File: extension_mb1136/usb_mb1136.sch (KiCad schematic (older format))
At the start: 20 parts, among them J1 Conn_01x03, J2 Conn_01x03, Q1 S9013, U1 STMPS2151MTR, U2 USBLC6-2

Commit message: add connector, develop pcb
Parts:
- added CNUSB_?: USB_B, Connector_USB:USB_B_OST_USB-B1HSxx_Horizontal, symbol Connector:USB_B
- renumbered C1 to C?, CNUSB_1 to CNUSB_?, CNUSB_2 to CNUSB_?, D1 to D?, LD1 to LD?, LD2 to LD?, Q1 to Q?, R1 to R?, R2 to R?, R5 to R?, R7 to R?, R4 to R?, R6 to R?, R8 to R?, R3 to R?, R9 to R?, U2 to U?, U1 to U?
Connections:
- net GND: now also CNUSB_?.4 (GND), CNUSB_?.5 (Shield)
- net at CNUSB_?.2 (D-), CNUSB_?.2 (D-), U?.4 (DMOUT): now also CNUSB_?.2 (D-)
- net at CNUSB_?.3 (D+), CNUSB_?.3 (D+), U?.6 (DPOUT): now also CNUSB_?.3 (D+)
- net VBUS renamed PA9
- net PA9: now also CNUSB_?.1 (VBUS)
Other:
- moved on the sheet: CNUSB_?

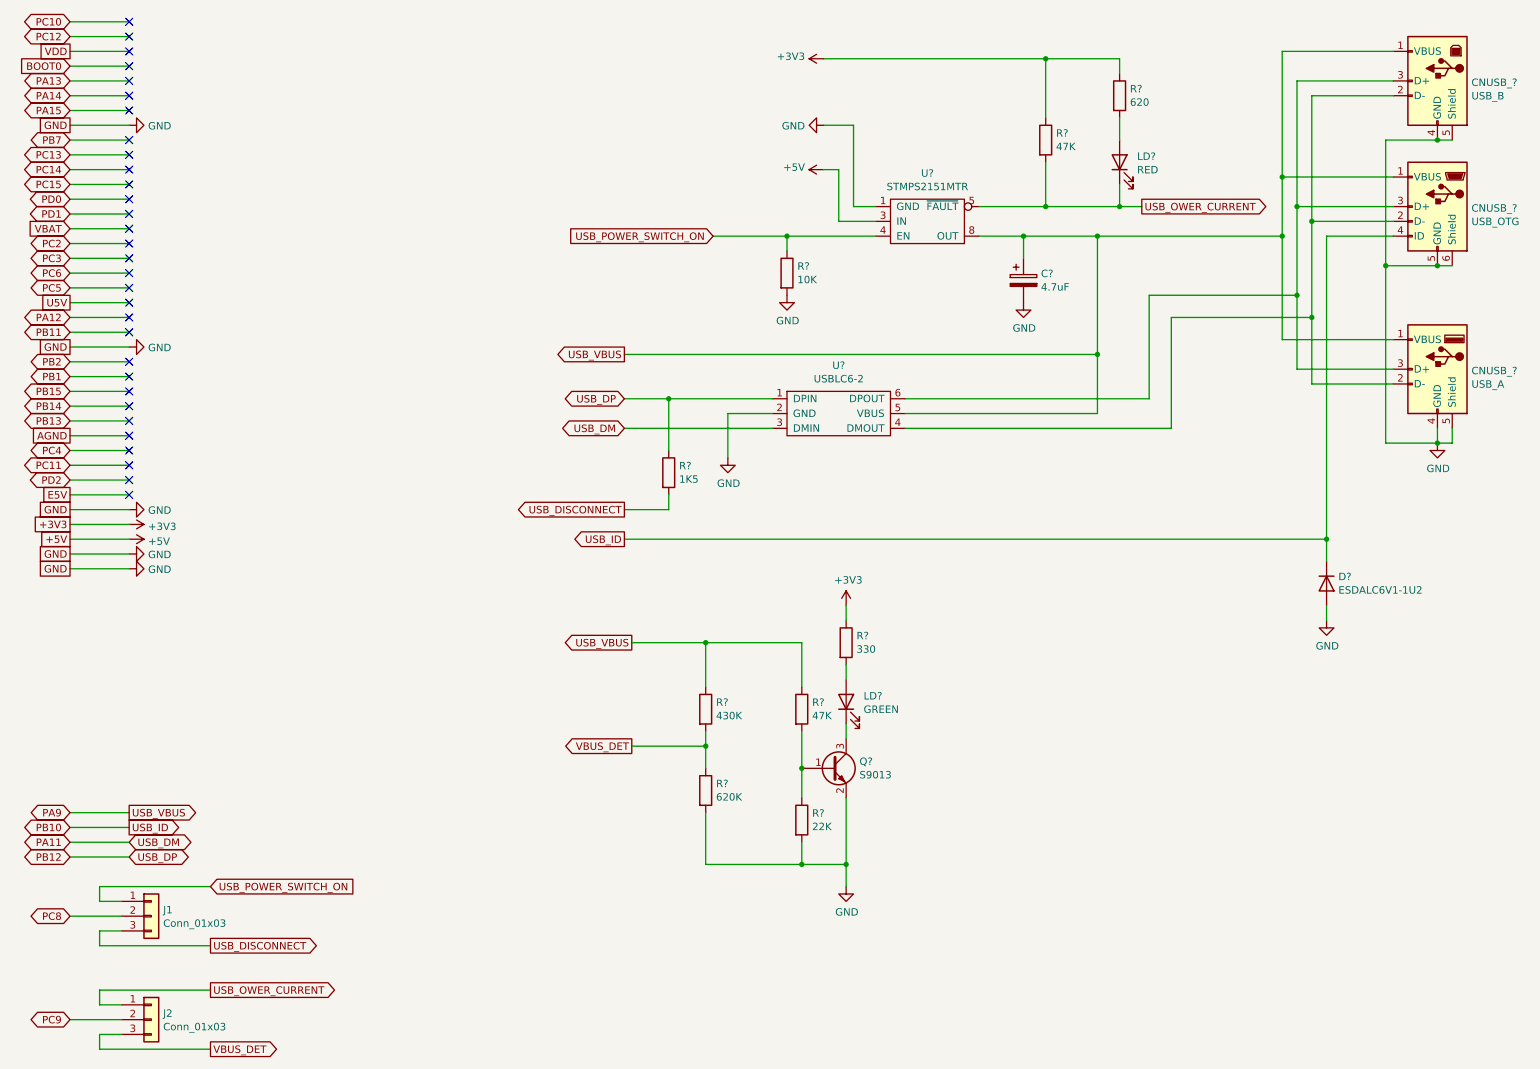
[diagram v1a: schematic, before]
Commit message: restore number of element
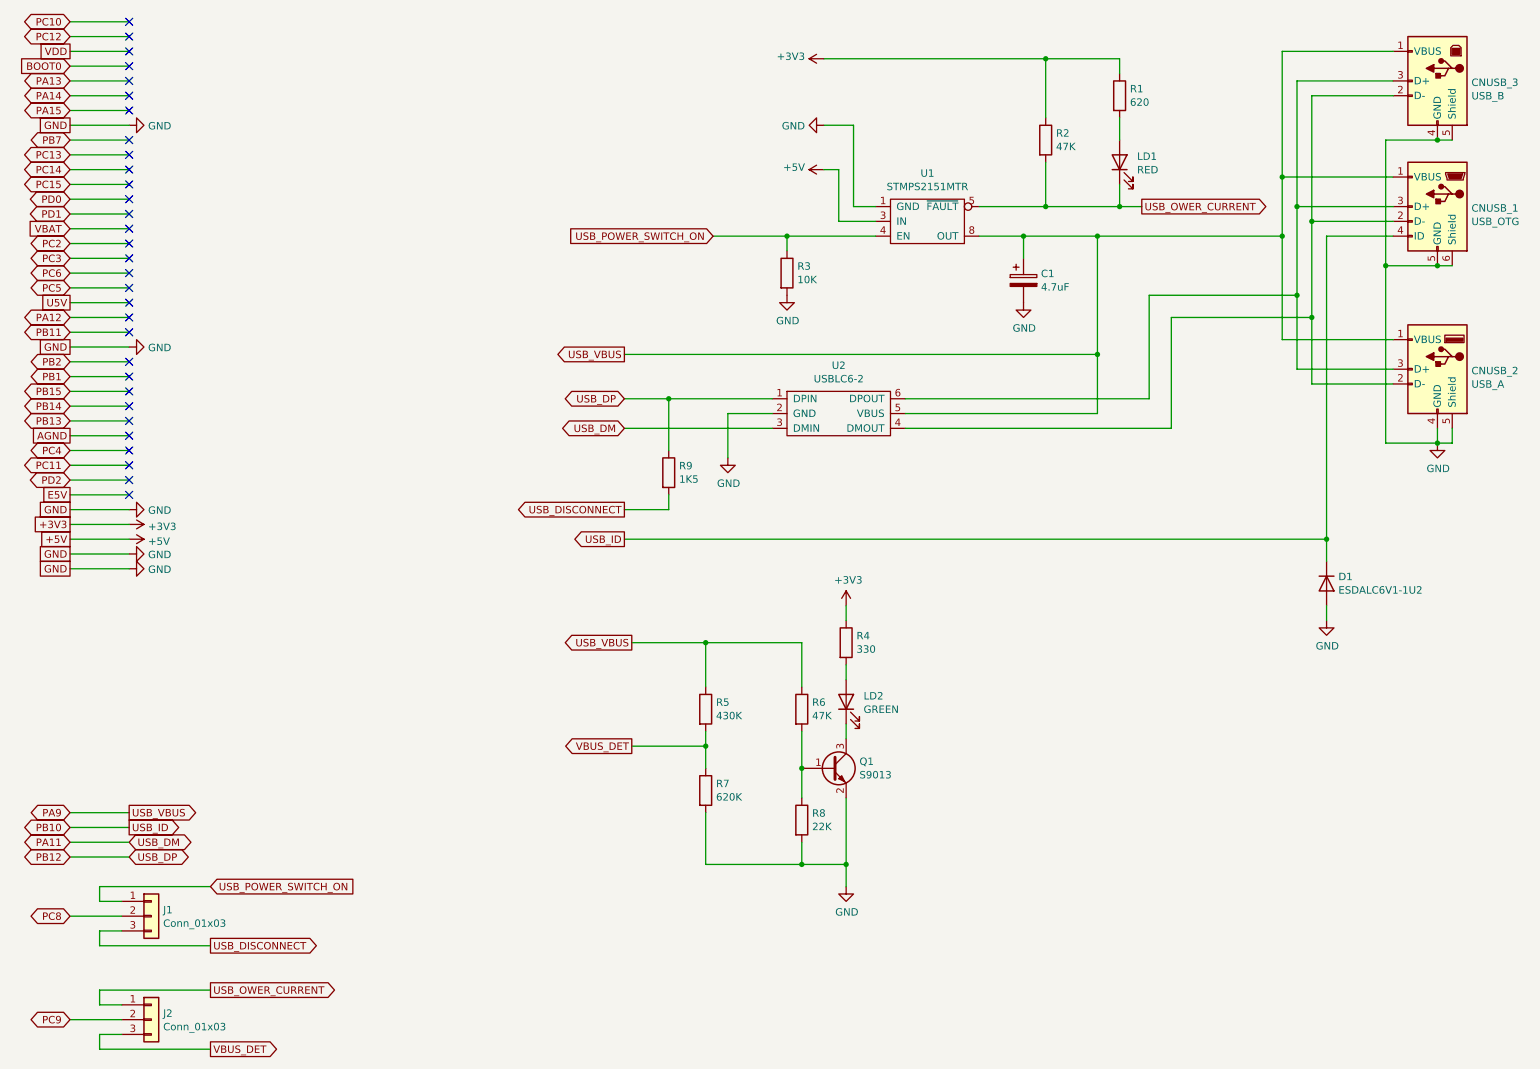
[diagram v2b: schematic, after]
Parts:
- gave numbers to parts that had none: 19
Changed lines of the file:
@@
 $EndDescr
 $Comp
-L Connector:USB_OTG CNUSB_?
+L Connector:USB_OTG CNUSB_1
 U 1 1 5FBD271C
 P 10150 1900
-F 0 "CNUSB_?" H 9920 1889 50  0000 R CNN
+F 0 "CNUSB_1" H 9920 1889 50  0000 R CNN
 F 1 "USB_OTG" H 9920 1798 50  0000 R CNN
 F 2 "Connector_USB:USB_Micro-B_Molex-105017-0001" H 10300 1850 50  0001 C CNN
@@
 USB_POWER_SWITCH_ON
 $Comp
-L Connector:USB_A CNUSB_?
+L Connector:USB_A CNUSB_2
 U 1 1 5FF0ECB3
 P 10150 3000
-F 0 "CNUSB_?" H 9920 2989 50  0000 R CNN
+F 0 "CNUSB_2" H 9920 2989 50  0000 R CNN
 F 1 "USB_A" H 9920 2898 50  0000 R CNN
 F 2 "Connector_USB:USB_A_Molex_67643_Horizontal" H 10300 2950 50  0001 C CNN
@@
 	10250 3500 10150 3500
 $Comp
-L Device:R R?
+L Device:R R1
 U 1 1 5FF1C87A
 P 8000 1150
-F 0 "R?" H 8070 1196 50  0000 L CNN
+F 0 "R1" H 8070 1196 50  0000 L CNN
 F 1 "620" H 8070 1105 50  0000 L CNN
 F 2 "Resistor_SMD:R_0805_2012Metric" V 7930 1150 50  0001 C CNN
@@
 $EndComp
 $Comp
-L Device:CP C?
+L Device:CP C1
 U 1 1 5FF205B2
 P 7350 2400
-F 0 "C?" H 7468 2446 50  0000 L CNN
+F 0 "C1" H 7468 2446 50  0000 L CNN
 F 1 "4.7uF" H 7468 2355 50  0000 L CNN
 F 2 "Capacitor_SMD:C_1206_3216Metric" H 7388 2250 50  0001 C CNN
@@
 $EndComp
 $Comp
-L power:GND #PWR?
+L power:GND #PWR0106
 U 1 1 5FF233E8
 P 7350 2550
-F 0 "#PWR?" H 7350 2300 50  0001 C CNN
+F 0 "#PWR0106" H 7350 2300 50  0001 C CNN
 F 1 "GND" H 7355 2377 50  0000 C CNN
 F 2 "" H 7350 2550 50  0001 C CNN
@@
 Connection ~ 7350 2100
 $Comp
-L Device:LED LD?
+L Device:LED LD1
 U 1 1 5FF25C2F
 P 8000 1600
-F 0 "LD?" V 8039 1482 50  0000 R CNN
+F 0 "LD1" V 8039 1482 50  0000 R CNN
 F 1 "RED" V 7948 1482 50  0000 R CNN
 F 2 "Diode_SMD:D_0805_2012Metric" H 8000 1600 50  0001 C CNN
@@
 Connection ~ 8000 1900
 $Comp
-L Device:R R?
+L Device:R R2
 U 1 1 5FF305D1
 P 7500 1450
-F 0 "R?" H 7570 1496 50  0000 L CNN
+F 0 "R2" H 7570 1496 50  0000 L CNN
 F 1 "47K" H 7570 1405 50  0000 L CNN
 F 2 "Resistor_SMD:R_0805_2012Metric" V 7430 1450 50  0001 C CNN
@@
 	7500 900  7500 1300
 $Comp
-L Device:R R?
+L Device:R R5
 U 1 1 5FF38FC2
 P 5200 5300
-F 0 "R?" H 5270 5346 50  0000 L CNN
+F 0 "R5" H 5270 5346 50  0000 L CNN
 F 1 "430K" H 5270 5255 50  0000 L CNN
 F 2 "Resistor_SMD:R_0805_2012Metric" V 5130 5300 50  0001 C CNN
@@
 $EndComp
 $Comp
-L Device:R R?
+L Device:R R7
 U 1 1 5FF3EEB0
 P 5200 5850
-F 0 "R?" H 5270 5896 50  0000 L CNN
+F 0 "R7" H 5270 5896 50  0000 L CNN
 F 1 "620K" H 5270 5805 50  0000 L CNN
 F 2 "Resistor_SMD:R_0805_2012Metric" V 5130 5850 50  0001 C CNN
@@
 VBUS_DET
 $Comp
-L Device:Q_NPN_BEC Q?
+L Device:Q_NPN_BEC Q1
 U 1 1 5FF6C39D
 P 6050 5700
-F 0 "Q?" H 6240 5746 50  0000 L CNN
+F 0 "Q1" H 6240 5746 50  0000 L CNN
 F 1 "S9013" H 6240 5655 50  0000 L CNN
 F 2 "Package_TO_SOT_SMD:SOT-23" H 6250 5800 50  0001 C CNN
@@
 Connection ~ 7850 2100
 $Comp
-L Device:R R?
+L Device:R R4
 U 1 1 5FF7C0A5
 P 6150 4850
-F 0 "R?" H 6220 4896 50  0000 L CNN
+F 0 "R4" H 6220 4896 50  0000 L CNN
 F 1 "330" H 6220 4805 50  0000 L CNN
 F 2 "Resistor_SMD:R_0805_2012Metric" V 6080 4850 50  0001 C CNN
@@
 $EndComp
 $Comp
-L Device:LED LD?
+L Device:LED LD2
 U 1 1 5FF7C0AB
 P 6150 5250
-F 0 "LD?" V 6189 5132 50  0000 R CNN
+F 0 "LD2" V 6189 5132 50  0000 R CNN
 F 1 "GREEN" V 6098 5132 50  0000 R CNN
 F 2 "Diode_SMD:D_0805_2012Metric" H 6150 5250 50  0001 C CNN
@@
 $EndComp
 $Comp
-L Device:R R?
+L Device:R R6
 U 1 1 5FF89CAE
 P 5850 5300
-F 0 "R?" H 5920 5346 50  0000 L CNN
+F 0 "R6" H 5920 5346 50  0000 L CNN
 F 1 "47K" H 5920 5255 50  0000 L CNN
 F 2 "Resistor_SMD:R_0805_2012Metric" V 5780 5300 50  0001 C CNN
@@
 	9100 2800 9100 2100
 $Comp
-L power:+3V3 #PWR?
+L power:+3V3 #PWR0101
 U 1 1 5FFAAE95
 P 6150 4600
-F 0 "#PWR?" H 6150 4450 50  0001 C CNN
+F 0 "#PWR0101" H 6150 4450 50  0001 C CNN
 F 1 "+3V3" H 6165 4773 50  0000 C CNN
 F 2 "" H 6150 4600 50  0001 C CNN
@@
 	6150 4600 6150 4700
 $Comp
-L power:GND #PWR?
+L power:GND #PWR0101
 U 1 1 5FFB903B
 P 6150 6500
-F 0 "#PWR?" H 6150 6250 50  0001 C CNN
+F 0 "#PWR0101" H 6150 6250 50  0001 C CNN
 F 1 "GND" H 6155 6327 50  0000 C CNN
 F 2 "" H 6150 6500 50  0001 C CNN
@@
 $EndComp
 $Comp
-L Device:R R?
+L Device:R R8
 U 1 1 5FFBBFDE
 P 5850 6050
-F 0 "R?" H 5920 6096 50  0000 L CNN
+F 0 "R8" H 5920 6096 50  0000 L CNN
 F 1 "22K" H 5920 6005 50  0000 L CNN
 F 2 "Resistor_SMD:R_0805_2012Metric" V 5780 6050 50  0001 C CNN
@@
 	5250 2100 5750 2100
 $Comp
-L Device:R R?
+L Device:R R3
 U 1 1 60084099
 P 5750 2350
-F 0 "R?" H 5820 2396 50  0000 L CNN
+F 0 "R3" H 5820 2396 50  0000 L CNN
 F 1 "10K" H 5820 2305 50  0000 L CNN
 F 2 "Resistor_SMD:R_0805_2012Metric" V 5680 2350 50  0001 C CNN
@@
 $EndComp
 $Comp
-L power:GND #PWR?
+L power:GND #PWR0111
 U 1 1 6008AD44
 P 5750 2500
-F 0 "#PWR?" H 5750 2250 50  0001 C CNN
+F 0 "#PWR0111" H 5750 2250 50  0001 C CNN
 F 1 "GND" H 5755 2327 50  0000 C CNN
 F 2 "" H 5750 2500 50  0001 C CNN
@@
 	9400 4150 4650 4150
 $Comp
-L Device:D D?
+L Device:D D1
 U 1 1 600DB0FD
 P 9400 4450
-F 0 "D?" V 9354 4530 50  0000 L CNN
+F 0 "D1" V 9354 4530 50  0000 L CNN
 F 1 "ESDALC6V1-1U2" V 9445 4530 50  0000 L CNN
 F 2 "Diode_SMD:D_0201_0603Metric" H 9400 4450 50  0001 C CNN
@@
 Connection ~ 9400 4150
 $Comp
-L power:GND #PWR?
+L power:GND #PWR0114
 U 1 1 600E78F0
 P 9400 4700
-F 0 "#PWR?" H 9400 4450 50  0001 C CNN
+F 0 "#PWR0114" H 9400 4450 50  0001 C CNN
 F 1 "GND" H 9405 4527 50  0000 C CNN
 F 2 "" H 9400 4700 50  0001 C CNN
@@
 	6550 3400 8350 3400
 $Comp
-L power:GND #PWR?
+L power:GND #PWR0115
 U 1 1 5FBFE674
 P 5350 3600
-F 0 "#PWR?" H 5350 3350 50  0001 C CNN
+F 0 "#PWR0115" H 5350 3350 50  0001 C CNN
 F 1 "GND" H 5355 3427 50  0000 C CNN
 F 2 "" H 5350 3600 50  0001 C CNN
@@
 	4650 2900 7850 2900
 $Comp
-L st:USBLC6-2 U?
+L st:USBLC6-2 U2
 U 1 1 5FBFF8BC
 P 6100 3300
-F 0 "U?" H 6100 3625 50  0000 C CNN
+F 0 "U2" H 6100 3625 50  0000 C CNN
 F 1 "USBLC6-2" H 6100 3534 50  0000 C CNN
 F 2 "Package_TO_SOT_SMD:SOT-23-6_Handsoldering" H 6100 3050 50  0001 C CNN
@@
 PC9
 $Comp
-L Connector_Generic:Conn_01x03 J?
+L Connector_Generic:Conn_01x03 J1
 U 1 1 5FD500E2
 P 1450 6700
-AR Path="/5FBD0F73/5FD500E2" Ref="J?"  Part="1"
+AR Path="/5FBD0F73/5FD500E2" Ref="J1"  Part="1"
 AR Path="/5FBD0FDB/5FD500E2" Ref="J1"  Part="1"
 F 0 "J1" H 1530 6742 50  0000 L CNN
@@
 $EndComp
 $Comp
-L Connector_Generic:Conn_01x03 J?
+L Connector_Generic:Conn_01x03 J2
 U 1 1 5FD500E8
 P 1450 7400
-AR Path="/5FBD0F73/5FD500E8" Ref="J?"  Part="1"
+AR Path="/5FBD0F73/5FD500E8" Ref="J2"  Part="1"
 AR Path="/5FBD0FDB/5FD500E8" Ref="J2"  Part="1"
 F 0 "J2" H 1530 7442 50  0000 L CNN
@@
 	1100 7600 1850 7600
 $Comp
-L power:GND #PWR?
+L power:GND #PWR0113
 U 1 1 6008FA5B
 P 6000 1350
-F 0 "#PWR?" H 6000 1100 50  0001 C CNN
+F 0 "#PWR0113" H 6000 1100 50  0001 C CNN
 F 1 "GND" V 6005 1222 50  0000 R CNN
 F 2 "" H 6000 1350 50  0001 C CNN
@@
 $EndComp
 $Comp
-L power:GND #PWR?
+L power:GND #PWR0120
 U 1 1 5FEBDF66
 P 1300 1350
-F 0 "#PWR?" H 1300 1100 50  0001 C CNN
+F 0 "#PWR0120" H 1300 1100 50  0001 C CNN
 F 1 "GND" V 1305 1222 50  0000 R CNN
 F 2 "" H 1300 1350 50  0001 C CNN
@@
 NoConn ~ 1300 2350
 $Comp
-L power:GND #PWR?
+L power:GND #PWR0121
 U 1 1 6012303E
 P 1300 2850
-F 0 "#PWR?" H 1300 2600 50  0001 C CNN
+F 0 "#PWR0121" H 1300 2600 50  0001 C CNN
 F 1 "GND" V 1305 2722 50  0000 R CNN
 F 2 "" H 1300 2850 50  0001 C CNN
@@
 USB_DISCONNECT
 $Comp
-L Device:R R?
+L Device:R R9
 U 1 1 60156F63
 P 4950 3700
-F 0 "R?" H 5020 3746 50  0000 L CNN
+F 0 "R9" H 5020 3746 50  0000 L CNN
 F 1 "1K5" H 5020 3655 50  0000 L CNN
 F 2 "Resistor_SMD:R_0805_2012Metric" V 4880 3700 50  0001 C CNN
@@
 	900  4250 1300 4250
 $Comp
-L power:GND #PWR?
+L power:GND #PWR0119
 U 1 1 5FE83AAA
 P 1300 4350
-F 0 "#PWR?" H 1300 4100 50  0001 C CNN
+F 0 "#PWR0119" H 1300 4100 50  0001 C CNN
 F 1 "GND" V 1305 4222 50  0000 R CNN
 F 2 "" H 1300 4350 50  0001 C CNN
@@
 $EndComp
 $Comp
-L power:GND #PWR?
+L power:GND #PWR0118
 U 1 1 5FE7D054
 P 1300 4250
-F 0 "#PWR?" H 1300 4000 50  0001 C CNN
+F 0 "#PWR0118" H 1300 4000 50  0001 C CNN
 F 1 "GND" V 1305 4122 50  0000 R CNN
 F 2 "" H 1300 4250 50  0001 C CNN
@@
 $EndComp
 $Comp
-L power:+3V3 #PWR?
+L power:+3V3 #PWR0103
 U 1 1 5FE3CDF5
 P 1300 4050
-F 0 "#PWR?" H 1300 3900 50  0001 C CNN
+F 0 "#PWR0103" H 1300 3900 50  0001 C CNN
 F 1 "+3V3" V 1315 4178 50  0000 L CNN
 F 2 "" H 1300 4050 50  0001 C CNN
@@
 $EndComp
 $Comp
-L power:GND #PWR?
+L power:GND #PWR0102
 U 1 1 5FE04097
 P 1300 3950
-F 0 "#PWR?" H 1300 3700 50  0001 C CNN
+F 0 "#PWR0102" H 1300 3700 50  0001 C CNN
 F 1 "GND" V 1305 3822 50  0000 R CNN
 F 2 "" H 1300 3950 50  0001 C CNN
@@
 $EndComp
 $Comp
-L power:+5V #PWR?
+L power:+5V #PWR0112
 U 1 1 5FDE4076
 P 1300 4150
-F 0 "#PWR?" H 1300 4000 50  0001 C CNN
+F 0 "#PWR0112" H 1300 4000 50  0001 C CNN
 F 1 "+5V" V 1315 4278 50  0000 L CNN
 F 2 "" H 1300 4150 50  0001 C CNN
@@
 	6000 1350 6200 1350
 $Comp
-L power:+3V3 #PWR?
+L power:+3V3 #PWR0108
 U 1 1 6030474E
 P 6000 900
-F 0 "#PWR?" H 6000 750 50  0001 C CNN
+F 0 "#PWR0108" H 6000 750 50  0001 C CNN
 F 1 "+3V3" V 6015 1028 50  0000 L CNN
 F 2 "" H 6000 900 50  0001 C CNN
@@
 	6000 1650 6100 1650
 $Comp
-L power:+5V #PWR?
+L power:+5V #PWR0107
 U 1 1 6008E133
 P 6000 1650
-F 0 "#PWR?" H 6000 1500 50  0001 C CNN
+F 0 "#PWR0107" H 6000 1500 50  0001 C CNN
 F 1 "+5V" V 6015 1778 50  0000 L CNN
 F 2 "" H 6000 1650 50  0001 C CNN
@@
 USB_DISCONNECT
 $Comp
-L st:STMPS2151MTR U?
+L st:STMPS2151MTR U1
 U 1 1 5FC6B1F4
 P 6700 2000
-F 0 "U?" H 6700 2325 50  0000 C CNN
+F 0 "U1" H 6700 2325 50  0000 C CNN
 F 1 "STMPS2151MTR" H 6700 2234 50  0000 C CNN
 F 2 "Package_SO:SO-8_3.9x4.9mm_P1.27mm" H 6800 1700 50  0001 C CNN
@@
 $EndComp
 $Comp
-L Connector:USB_B CNUSB_?
+L Connector:USB_B CNUSB_3
 U 1 1 5FFEEA84
 P 10150 1050
-F 0 "CNUSB_?" H 9920 1039 50  0000 R CNN
+F 0 "CNUSB_3" H 9920 1039 50  0000 R CNN
 F 1 "USB_B" H 9920 948 50  0000 R CNN
 F 2 "Connector_USB:USB_B_OST_USB-B1HSxx_Horizontal" H 10300 1000 50  0001 C CNN
